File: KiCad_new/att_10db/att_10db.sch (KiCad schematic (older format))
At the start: 6 parts

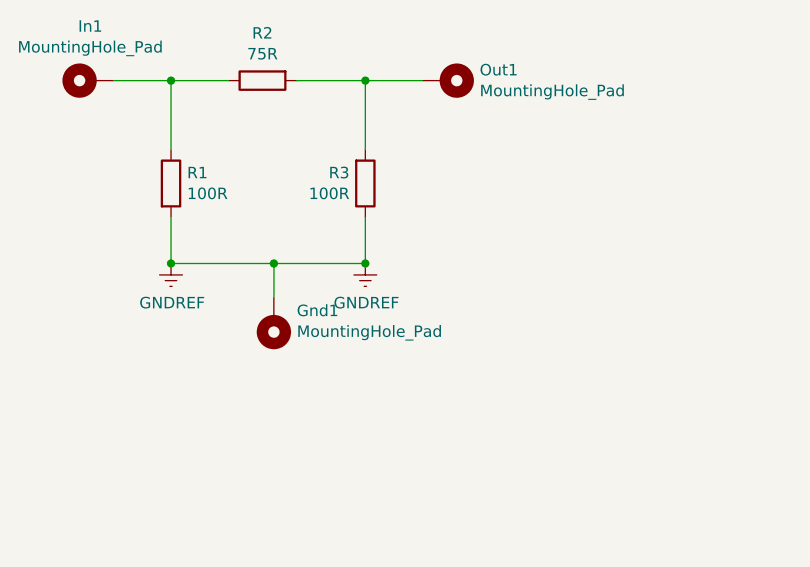
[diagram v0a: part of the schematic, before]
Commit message: One more GND pad dded
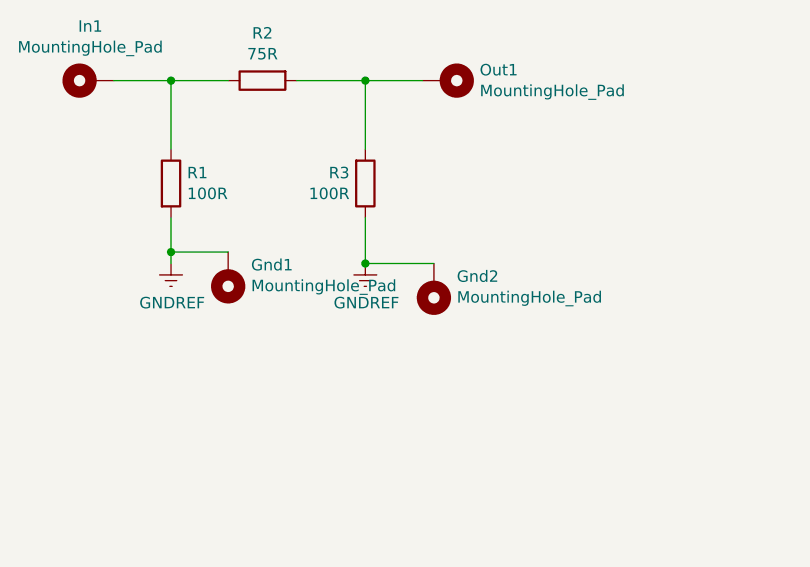
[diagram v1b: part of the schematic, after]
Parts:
- added Gnd2: MountingHole_Pad, TestPoint:TestPoint_Pad_2.5x2.5mm, symbol Mechanical:MountingHole_Pad
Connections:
- net GNDREF: now also Gnd2.1
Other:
- moved on the sheet: Gnd1
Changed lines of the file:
@@
 $EndComp
 Wire Wire Line
-	3650 3850 3650 4050
+	3650 3850 3650 4000
 Wire Wire Line
 	4500 3850 4500 4050
@@
 L Mechanical:MountingHole_Pad Gnd1
 U 1 1 5E248D13
-P 4100 4300
-F 0 "Gnd1" H 4000 4257 50  0000 R CNN
-F 1 "MountingHole_Pad" H 4000 4348 50  0000 R CNN
-F 2 "TestPoint:TestPoint_Pad_2.5x2.5mm" H 4100 4300 50  0001 C CNN
-F 3 "~" H 4100 4300 50  0001 C CNN
-	1    4100 4300
+P 3900 4100
+F 0 "Gnd1" H 3800 4057 50  0000 R CNN
+F 1 "MountingHole_Pad" H 3800 4148 50  0000 R CNN
+F 2 "TestPoint:TestPoint_Pad_2.5x2.5mm" H 3900 4100 50  0001 C CNN
+F 3 "~" H 3900 4100 50  0001 C CNN
+	1    3900 4100
 	-1   0    0    1
 $EndComp
-Wire Wire Line
-	3650 4050 4100 4050
-Wire Wire Line
-	4100 4050 4100 4200
-Connection ~ 3650 4050
-Wire Wire Line
-	4100 4050 4500 4050
-Connection ~ 4100 4050
-Connection ~ 4500 4050
 Wire Wire Line
 	4750 3250 4500 3250
@@
 Text Notes 1000 950  0    50   ~ 0
 All Resistors TO-220 /50W /Non Inductive
+Wire Wire Line
+	3900 4000 3650 4000
+Connection ~ 3650 4000
+Wire Wire Line
+	3650 4000 3650 4050
+$Comp
+L Mechanical:MountingHole_Pad Gnd2
+U 1 1 5E247856
+P 4800 4150
+F 0 "Gnd2" H 4700 4107 50  0000 R CNN
+F 1 "MountingHole_Pad" H 4700 4198 50  0000 R CNN
+F 2 "TestPoint:TestPoint_Pad_2.5x2.5mm" H 4800 4150 50  0001 C CNN
+F 3 "~" H 4800 4150 50  0001 C CNN
+	1    4800 4150
+	-1   0    0    1
+$EndComp
+Wire Wire Line
+	4800 4050 4500 4050
+Connection ~ 4500 4050
 $EndSCHEMATC
